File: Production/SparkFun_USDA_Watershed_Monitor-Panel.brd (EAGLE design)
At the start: 77.2 x 102.9 mm, 239 parts, among them J10 QWIIC_RIGHT_ANGLE, J3 QWIIC_RIGHT_ANGLE, J4 U.FL, J5 RJ45, J7 RJ45, J9 RJ45, Q1 20V/4.2A/52mΩ/1.4W, Q2 20V/0.2A/8MHz/1.2Ω/1Vth, Q3 20V/0.2A/8MHz/1.2Ω/1Vth, Q4 20V/0.2A/8MHz/1.2Ω/1Vth, Q5 20V/4.2A/52mΩ/1.4W, Q7 20V/4.2A/52mΩ/1.4W, U1 ESP-WROOM-3232D, U10 MMC5983MA_QFN16, U11 RFM9XRFM95, U12 NAU7802SOIC, U2 AP3429A, U3 MCP73831, U5 BME680, U6 9DoF IMU, U7 1.8V/100mA, U8 CH340C, U9 ISM330DHCX

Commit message: Add v10 production files
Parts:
- added BME_ADR1, BME_ADR2, BME_ADR3, BME_ADR4, BME_ADR5, CHG1, CHG2, CHG3, CHG4, CHG5, NAU_CAP1, NAU_CAP2, NAU_CAP3, NAU_CAP4, NAU_CAP5, PWR1, PWR2, PWR3, PWR4, PWR5, SHLD1, SHLD2, SHLD3, SHLD4, SHLD5: JUMPER-SMT_2_NC_TRACE_SILK, SparkFun-Jumpers:SMT-JUMPER_2_NC_TRACE_SILK
- added BOOT1, BOOT2, BOOT3, BOOT4, BOOT5, RESET1, RESET2, RESET3, RESET4, RESET5: MOMENTARY-SWITCH-SPST-SMD-4.6X2.8MM, SparkFun-Switches:TACTILE_SWITCH_SMD_4.6X2.8MM
- added C100, C101, C124, C125, C28, C29, C52, C53, C76, C77: 4.7uF, SparkFun-Capacitors:0603
- added C102, C103, C106, C107, C108, C109, C114, C115, C117, C126, C127, C130, C131, C132, C133, C138, C139, C141, C30, C31, C34, C35, C36, C37, C42, C43, C45, C54, C55, C58, C59, C60, C61, C66, C67, C69, C78, C79, C82, C83, C84, C85, C90, C91, C93: 0.1uF, SparkFun-Capacitors:0603
- added C104, C105, C128, C129, C32, C33, C56, C57, C80, C81: 1.0uF, SparkFun-Capacitors:0603
- added C110, C111, C112, C113, C134, C135, C136, C137, C38, C39, C40, C41, C62, C63, C64, C65, C86, C87, C88, C89: DNP, SparkFun-Capacitors:0603
- added C116, C140, C44, C68, C92: 330pF, SparkFun-Capacitors:0603
- added C118, C142, C46, C70, C94: 10uF, SparkFun-Capacitors:0603
- added C119, C121, C122, C143, C25, C26, C47, C49, C50, C71, C73, C74, C95, C97, C98: 22uF, SparkFun-Capacitors:0805
- added C120, C144, C48, C72, C96: 10nF, SparkFun-Capacitors:0603
- added C123, C27, C51, C75, C99: 22pF, SparkFun-Capacitors:0603
- added D10, D16, D22, D28, D34: BLUE, SparkFun-LED:LED-0603
- added D11, D12, D13, D17, D18, D19, D23, D24, D25, D29, D30, D31, D35, D36, D7: 3A/10V/280mV, SparkFun-DiscreteSemi:SOD-323
- added D14, D20, D26, D32, D8: DNP, SparkFun-LED:LED-0603
- added D15, D21, D27, D33, D9: Yellow, SparkFun-LED:LED-0603
- added FD10, FD11, FD12, FD13, FD14, FD15, FD16, FD17, FD18, FD19, FD20, FD21, FD22, FD23, FD24, FD5, FD6, FD7, FD8, FD9: FIDUCIAL1X2, SparkFun-Aesthetics:FIDUCIAL-1X2
- added H10, H11, H12, H13, H14, H15, H16, H17, H18, H19, H20, H21, H22, H23, H24, H5, H6, H7, H8, H9: STAND-OFF, SparkFun-Hardware:STAND-OFF
- added I2C1, I2C2, I2C3, I2C4, I2C5: JUMPER-SMT_3_2-NC_TRACE_SILK, SparkFun-Jumpers:SMT-JUMPER_3_2-NC_TRACE_SILK
- added ICM_ADR1, ICM_ADR2, ICM_ADR3, ICM_ADR4, ICM_ADR5, ISM_ADR1, ISM_ADR2, ISM_ADR3, ISM_ADR4, ISM_ADR5: JUMPER-SMT_2_NO_SILK, SparkFun-Jumpers:SMT-JUMPER_2_NO_SILK
- added ICM_INT1, ICM_INT2, ICM_INT3, ICM_INT4, ICM_INT5, ISM_INT10, ISM_INT11, ISM_INT12, ISM_INT3, ISM_INT4, ISM_INT5, ISM_INT6, ISM_INT7, ISM_INT8, ISM_INT9, MMC_INT1, MMC_INT2, MMC_INT3, MMC_INT4, MMC_INT5, NAU_INT1, NAU_INT2, NAU_INT3, NAU_INT4, NAU_INT5: JUMPER-SMT_3_1-NC_TRACE_SILK, SparkFun-Jumpers:SMT-JUMPER_3_1-NC_TRACE_SILK
- added J12, J24, J36, J48, J60, J72: 3-PIN SMD, SparkFun-Connectors:JST-3-SMD
- added J13, J25, J37, J49, J61: (no value), SparkFun-Connectors:USB-C-16P-2LAYER-PADS
- added J14, J26, J38, J50, J62: (no value), SparkFun-Connectors:JST-2-SMD
- added J15, J21, J27, J33, J39, J45, J51, J57, J63, J69: QWIIC_RIGHT_ANGLE, SparkFun-Connectors:JST04_1MM_RA
- added J16, J28, J40, J52, J64: U.FL, SparkFun-Connectors:U.FL
- added J17, J23, J29, J35, J41, J47, J53, J59, J65, J71: (no value), SparkFun-Connectors:1X02_NO_SILK
- added J18, J19, J20, J30, J31, J32, J42, J43, J44, J54, J55, J56, J66, J67, J68: RJ45, SparkFun-Connectors:RJ45-8
- added J22, J34, J46, J58, J70: (no value), SparkFun-Connectors:1X04_NO_SILK
- added L2, L3, L4, L5, L6: 2.2μH, SparkFun-Coils:INDUCTOR_4X4MM
- added LOGO10, LOGO11, LOGO15, LOGO16, LOGO20, LOGO21, LOGO25, LOGO26, LOGO30, LOGO6: SFE_LOGO_NAME_FLAME.1_INCH, SparkFun-Aesthetics:SFE_LOGO_NAME_FLAME_.1
- added LOGO12, LOGO17, LOGO22, LOGO27, LOGO7: OSHW-LOGOS, SparkFun-Aesthetics:OSHW-LOGO-S
- added LOGO13, LOGO14, LOGO18, LOGO19, LOGO23, LOGO24, LOGO28, LOGO29, LOGO8, LOGO9: QWIIC_LOGO_4MM, SparkFun-Aesthetics:QWIIC_4MM
- added MEAS1, MEAS2, MEAS3, MEAS4, MEAS5: JUMPER-COMBO_2_NC_TRACE, SparkFun-Jumpers:COMBO-JUMPER_2_NC_TRACE
- added Q10, Q12, Q17, Q18, Q21, Q23, Q28, Q29, Q32, Q34, Q39, Q40, Q43, Q45, Q50, Q51, Q54, Q56, Q61, Q62, Q65: 20V/4.2A/52mΩ/1.4W, SparkFun-DiscreteSemi:SOT23-3
- added Q11, Q13, Q14, Q15, Q19, Q20, Q22, Q24, Q25, Q26, Q30, Q31, Q33, Q35, Q36, Q37, Q41, Q42, Q44, Q46, Q47, Q48, Q52, Q53, Q55, Q57, Q58, Q59, Q63, Q64, Q66, Q8, Q9: 20V/0.2A/8MHz/1.2Ω/1Vth, SparkFun-DiscreteSemi:SOT-416FL
- added Q16, Q27, Q38, Q49, Q60: (no value), SparkFun-DiscreteSemi:SC70-6
- added R100, R131, R162, R38, R69: 4.7k, SparkFun-Resistors:0603
- added R101, R103, R104, R107, R108, R116, R121, R122, R132, R134, R135, R138, R139, R147, R152, R153, R163, R165, R166, R169, R170, R178, R183, R184, R29, R30, R39, R41, R42, R45, R46, R54, R59, R60, R70, R72, R73, R76, R77, R85, R90, R91: 2.2k, SparkFun-Resistors:0603
- added R102, R111, R133, R142, R164, R173, R40, R49, R71, R80: DNP, SparkFun-Resistors:0603
- added R105, R106, R109, R110, R117, R118, R119, R120, R123, R124, R127, R128, R130, R136, R137, R140, R141, R148, R149, R150, R151, R154, R155, R158, R159, R161, R167, R168, R171, R172, R179, R180, R181, R182, R185, R186, R28, R31, R34, R35, R37, R43, R44, R47, R48, R55, R56, R57, R58, R61, R62, R65, R66, R68, R74, R75, R78, R79, R86, R87, R88, R89, R92, R93, R96, R97, R99: 100k, SparkFun-Resistors:0603
- added R112, R113, R143, R144, R174, R175, R50, R51, R81, R82: 47, SparkFun-Resistors:0603
- added R114, R115, R145, R146, R176, R177, R52, R53, R83, R84: 10k, SparkFun-Resistors:0603
- added R125, R126, R156, R157, R32, R33, R63, R64, R94, R95: 5.1k, SparkFun-Resistors:0603
- added R129, R160, R36, R67, R98: 453k, SparkFun-Resistors:0603
- added TP2, TP3, TP4, TP5, TP6: TEST-POINT3X4, SparkFun-Connectors:PAD.03X.04
- added U$119, U$207, U$330, U$453, U$576, U$699: (no value), output:0X770
- added U$120, U$208, U$331, U$454, U$577, U$700: (no value), output:0X760
- added U$121, U$125, U$205, U$209, U$213, U$328, U$332, U$336, U$451, U$455, U$459, U$574, U$578, U$582, U$697, U$701, U$705, U$82: (no value), output:OPEN#0
- added U$122, U$126, U$206, U$210, U$214, U$329, U$333, U$337, U$452, U$456, U$460, U$575, U$579, U$583, U$698, U$702, U$706, U$83: (no value), output:CLOSED#0
- added U$123, U$215, U$338, U$461, U$584, U$707: (no value), output:0X6A0
- added U$124, U$216, U$339, U$462, U$585, U$708: (no value), output:0X6B0
- added U$127, U$211, U$334, U$457, U$580, U$703: (no value), output:0X690
- added U$128, U$212, U$335, U$458, U$581, U$704: (no value), output:0X680
- added U$129, U$260, U$383, U$506, U$629: (no value), output:RESET0
- added U$130, U$261, U$384, U$507, U$630: (no value), output:BOOT0
- added U$131, U$262, U$385, U$508, U$631: (no value), output:PWR0
- added U$132, U$263, U$386, U$509, U$632: (no value), output:STAT0
- added U$133, U$264, U$387, U$510, U$633: (no value), output:IO20
- added U$134, U$265, U$388, U$511, U$634: (no value), output:ORW0
- added U$135, U$266, U$389, U$512, U$635: (no value), output:OR0
- added U$136, U$267, U$390, U$513, U$636: (no value), output:GRW0
- added U$137, U$220, U$224, U$343, U$347, U$466, U$470, U$589, U$593, U$712, U$716: (no value), output:ICM0
- added U$138, U$217, U$225, U$232, U$235, U$340, U$348, U$355, U$358, U$463, U$471, U$478, U$481, U$586, U$594, U$601, U$604, U$709, U$717, U$724, U$727: (no value), output:X0
- added U$139, U$218, U$226, U$233, U$236, U$341, U$349, U$356, U$359, U$464, U$472, U$479, U$482, U$587, U$595, U$602, U$605, U$710, U$718, U$725, U$728: (no value), output:Y0
- added U$140, U$219, U$227, U$234, U$237, U$342, U$350, U$357, U$360, U$465, U$473, U$480, U$483, U$588, U$596, U$603, U$606, U$711, U$719, U$726, U$729: (no value), output:Z0
- added U$141, U$142, U$228, U$229, U$351, U$352, U$474, U$475, U$597, U$598, U$720, U$721: (no value), output:MAG0
- added U$143, U$144, U$230, U$231, U$353, U$354, U$476, U$477, U$599, U$600, U$722, U$723: (no value), output:A#G0
- added U$145, U$268, U$391, U$514, U$637: (no value), output:GR0
- added U$146, U$269, U$392, U$515, U$638: (no value), output:BLW0
- added U$147, U$270, U$393, U$516, U$639: (no value), output:BL0
- added U$148, U$271, U$394, U$517, U$640: (no value), output:BRW0
- added U$149, U$272, U$395, U$518, U$641: (no value), output:BR0
- added U$150, U$151, U$153, U$273, U$274, U$276, U$396, U$397, U$399, U$519, U$520, U$522, U$642, U$643, U$645: (no value), output:GND0
- added U$152, U$245, U$275, U$368, U$398, U$491, U$521, U$614, U$644, U$737: (no value), output:3V30
- added U$154, U$277, U$400, U$523, U$646: (no value), output:VDD0
- added U$155, U$278, U$401, U$524, U$647: (no value), output:A#0
- added U$156, U$279, U$402, U$525, U$648: (no value), output:A#1
- added U$157, U$280, U$403, U$526, U$649: (no value), output:B#0
- added U$158, U$281, U$404, U$527, U$650: (no value), output:B#1
- added U$159, U$282, U$405, U$528, U$651: (no value), output:E#0
- added U$160, U$283, U$406, U$529, U$652: (no value), output:E#1
- added U$161, U$284, U$407, U$530, U$653: (no value), output:#RJ45_COLORS#0
- added U$162, U$285, U$408, U$531, U$654: (no value), output:#PWR#0
- added U$163, U$286, U$409, U$532, U$655: (no value), output:IO250
- added U$164, U$287, U$410, U$533, U$656: (no value), output:IO330
- added U$165, U$288, U$411, U$534, U$657: (no value), output:IO170
- added U$166, U$289, U$412, U$535, U$658: (no value), output:IO180
- added U$167, U$290, U$413, U$536, U$659: (no value), output:IO190
- added U$168, U$291, U$414, U$537, U$660: (no value), output:I340
- added U$169, U$292, U$415, U$538, U$661: (no value), output:I350
- added U$170, U$293, U$416, U$539, U$662: (no value), output:I390
- added U$171, U$294, U$417, U$540, U$663: (no value), output:#IO19#0
- added U$172, U$295, U$418, U$541, U$664: (no value), output:#IO18#0
- added U$173, U$243, U$296, U$366, U$419, U$489, U$542, U$612, U$665, U$735: (no value), output:#IO17#0
- added U$174, U$297, U$420, U$543, U$666: (no value), output:#NAU_INT#0
- added U$175, U$298, U$421, U$544, U$667: (no value), output:#MMC_INT#0
- added U$176, U$299, U$422, U$545, U$668: (no value), output:#ISM_INT2#0
- added U$177, U$300, U$423, U$546, U$669: (no value), output:#ISM_INT1#0
- added U$178, U$301, U$424, U$547, U$670: (no value), output:#ICM_INT#0
- added U$179, U$302, U$425, U$548, U$671: (no value), output:#IO#0
- added U$180, U$303, U$426, U$549, U$672: (no value), output:##INT##0
- added U$181, U$304, U$427, U$550, U$673: (no value), output:#NOTES#0
- added U$182, U$305, U$428, U$551, U$674: (no value), output:IO230
- added U$183, U$185, U$306, U$308, U$429, U$431, U$552, U$554, U$675, U$677: (no value), output:#GND_#0
- added U$184, U$186, U$307, U$309, U$430, U$432, U$553, U$555, U$676, U$678: (no value), output:#_GND#0
- added U$187, U$310, U$433, U$556, U$679: (no value), output:#3V3_#0
- added U$188, U$311, U$434, U$557, U$680: (no value), output:#SDA_#0
- added U$189, U$312, U$435, U$558, U$681: (no value), output:#SCL_#0
- added U$190, U$313, U$436, U$559, U$682: (no value), output:#_SCL#1
- added U$191, U$314, U$437, U$560, U$683: (no value), output:#_SDA#2
- added U$192, U$315, U$438, U$561, U$684: (no value), output:#_3V3#0
- added U$193, U$196, U$316, U$319, U$439, U$442, U$562, U$565, U$685, U$688: (no value), output:#LOAD_CELL#0
- added U$194, U$197, U$317, U$320, U$440, U$443, U$563, U$566, U$686, U$689: (no value), output:#GPIO_A#0
- added U$195, U$198, U$318, U$321, U$441, U$444, U$564, U$567, U$687, U$690: (no value), output:#GPIO_B#0
- added U$199, U$247, U$322, U$370, U$445, U$493, U$568, U$616, U$691: (no value), output:USDA0
- added U$200, U$248, U$323, U$371, U$446, U$494, U$569, U$617, U$692: (no value), output:WATERSHED0
- added U$201, U$249, U$324, U$372, U$447, U$495, U$570, U$618, U$693: (no value), output:MONITOR0
- added U$202, U$325, U$448, U$571, U$694: (no value), output:NC0
- added U$203, U$326, U$449, U$572, U$695: (no value), output:#5V_IN_#0
- added U$204, U$327, U$450, U$573, U$696: (no value), output:#_5V_IN#0
- added U$221, U$344, U$467, U$590, U$713: (no value), output:ISM0
- added U$222, U$345, U$468, U$591, U$714: (no value), output:MMC0
- added U$223, U$346, U$469, U$592, U$715: (no value), output:IMU_AXES0
- added U$238, U$361, U$484, U$607, U$730: (no value), output:I360
- added U$239, U$362, U$485, U$608, U$731: (no value), output:VOUT0
- added U$240, U$363, U$486, U$609, U$732: (no value), output:#GPS#0
- added U$241, U$364, U$487, U$610, U$733: (no value), output:GND3
- added U$242, U$246, U$365, U$369, U$488, U$492, U$611, U$615, U$734, U$738: (no value), output:VO0
- added U$244, U$367, U$490, U$613, U$736: (no value), output:#IO23#0
- added U$250, U$373, U$496, U$619: (no value), output:#MEAS#0
- added U$251, U$374, U$497, U$620: (no value), output:#CHG#0
- added U$252, U$375, U$498, U$621: (no value), output:#I2C#0
- added U$253, U$376, U$499, U$622: (no value), output:CHG0
- added U$254, U$377, U$500, U$623: (no value), output:#CAP#0
- added U$255, U$378, U$501, U$624: (no value), output:#BME_ADR#0
- added U$256, U$379, U$502, U$625: (no value), output:#ICM_ADR#0
- added U$257, U$380, U$503, U$626: (no value), output:#ISM_ADR#0
- added U$258, U$381, U$504, U$627: (no value), output:#BATTERY#0
- added U$259, U$382, U$505, U$628: (no value), output:#SHLD#0
- added U13, U24, U35, U46, U57: AP3429A, SparkFun-IC-Power:SOT23-5
- added U14, U25, U36, U47, U58: MCP73831, SparkFun-IC-Power:SOT23-5
- added U15, U26, U37, U48, U59: BME680, SparkFun-Sensors:LGA3.0X3.0
- added U16, U27, U38, U49, U60: 9DoF IMU, SparkFun-Sensors:QFN24-3X3-ICM-20948
- added U17, U28, U39, U50, U61: 1.8V/100mA, SparkFun-IC-Power:SC70
- added U18, U29, U40, U51, U62: CH340C, SparkFun-IC-Comms:SO016
- added U19, U30, U41, U52, U63: DNP, SparkFun-Sensors:LGA-14L
- added U20, U31, U42, U53, U64: DNP, SparkFun-Sensors:LGA-16-3X3MM-4X4PINS
- added U21, U32, U43, U54, U65: RFM9XRFM95, SparkFun-RF:RFM95
- added U22, U33, U44, U55, U66: NAU7802SOIC, SparkFun-IC-Conversion:SO16
- added U23, U34, U4, U45, U56: ESP-WROOM-3232D, SparkFun-RF:ESP-WROOM-32D
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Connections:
- net !RFM_CS! renamed ESP_IO15/!RFM_CS!
- net !RFM_RST! renamed ESP_IO5/!RFM_RST!
- net ESP_IO0_BOOT renamed ESP_IO0/BOOT
- net ESP_RX renamed ESP_IO3/ESP_RX
- net ESP_TX renamed ESP_IO1/ESP_TX
- net PICO renamed ESP_IO13/PICO
- net POCI renamed ESP_IO12/POCI
- net RFM_IO0 renamed ESP_IO27/RFM_IO0
- net RFM_IO1 renamed ESP_IO26/RFM_IO1
- net SCK renamed ESP_IO14/SCK
- net STAT renamed ESP_IO2/STAT
- net V_BATT_2 renamed ESP_IO32/V_BATT_2
- removed net ESP_I36: J7.5, U1.4
- removed net ESP_INT_COM: ICM_INT.3, ISM_INT1.3, ISM_INT2.3, MMC_INT.3, NAU_INT.3, U1.26
- removed net SCL: J10.4, J3.4, J8.1, Q3.3, R11.1, U1.36, U10.1, U12.13, U5.4, U9.P13
- removed net SDA: J10.3, J3.3, J8.2, Q2.3, R12.1, U1.33, U10.16, U12.14, U5.3, U9.P14
- new net 1.8V1: C33.1, C34.1, C35.1, Q13.1, Q14.1, R44.2, R45.2, R46.2, TP2.1, U16.13, U16.22, U16.8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
- new net 1.8V2: C57.1, C58.1, C59.1, Q24.1, Q25.1, R75.2, R76.2, R77.2, TP3.1, U27.13, U27.22, U27.8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
- new net 1.8V3: C81.1, C82.1, C83.1, Q35.1, Q36.1, R106.2, R107.2, R108.2, TP4.1, U38.13, U38.22, U38.8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
- new net 1.8V4: C105.1, C106.1, C107.1, Q46.1, Q47.1, R137.2, R138.2, R139.2, TP5.1, U49.13, U49.22, U49.8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
- new net 1.8V5: C129.1, C130.1, C131.1, Q57.1, Q58.1, R168.2, R169.2, R170.2, TP6.1, U60.13, U60.22, U60.8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
- new net 3.3V1: C26.1, C27.2, C47.1, D8.A, I2C1.2, J15.2, J19.7, J20.7, J22.3, L2.P$2, Q18.2, Q21.2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
- new net 3.3V2: C50.1, C51.2, C71.1, D14.A, I2C2.2, J27.2, J31.7, J32.7, J34.3, L3.P$2, Q29.2, Q32.2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
- new net 3.3V3: C74.1, C75.2, C95.1, D20.A, I2C3.2, J39.2, J43.7, J44.7, J46.3, L4.P$2, Q40.2, Q43.2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
- new net 3.3V4: C119.1, C98.1, C99.2, D26.A, I2C4.2, J51.2, J55.7, J56.7, J58.3, L5.P$2, Q51.2, Q54.2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
- new net 3.3V5: C122.1, C123.2, C143.1, D32.A, I2C5.2, J63.2, J67.7, J68.7, J70.3, L6.P$2, Q62.2, Q65.2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
- new net 3V3_EN1: R35.2, U13.1
- new net 3V3_EN2: R66.2, U24.1
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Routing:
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- added copper zone on layer 1, net 3.3V1
- added copper zone on layer 16, net 3.3V1
- added copper zone on layer 1, net 3.3V2
- added copper zone on layer 16, net 3.3V2
- added copper zone on layer 1, net 3.3V3
- added copper zone on layer 16, net 3.3V3
- added copper zone on layer 1, net 3.3V4
- added copper zone on layer 16, net 3.3V4
- added copper zone on layer 1, net 3.3V5
- added copper zone on layer 16, net 3.3V5
- added copper zone on layer 1, net GND1
- added copper zone on layer 16, net GND1
- added copper zone on layer 1, net GND10
- added copper zone on layer 16, net GND10
- added copper zone on layer 16, net GND11
- added copper zone on layer 16, net GND3
- added copper zone on layer 1, net GND4
- added copper zone on layer 16, net GND4
- added copper zone on layer 16, net GND5
- added copper zone on layer 1, net GND6
- added copper zone on layer 16, net GND6
- added copper zone on layer 16, net GND7
- added copper zone on layer 1, net GND8
- added copper zone on layer 16, net GND8
- added copper zone on layer 16, net GND9
- added copper zone on layer 1, net SHLD1
- added copper zone on layer 16, net SHLD1
- added copper zone on layer 1, net SHLD2
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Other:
- board size 77.2 x 102.9 mm -> 141.2 x 245.1 mm
- board text added: "v10"
- board text removed: "v01"

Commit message: Change DIO-14072 for DIO-11623
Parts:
- D1, D11, D12, D13, D17, D18, D19, D23, D24, D25, D29, D30, D31, D35, D36, D5, D6, D7: value 3A/10V/280mV -> 1A/23V/620mV

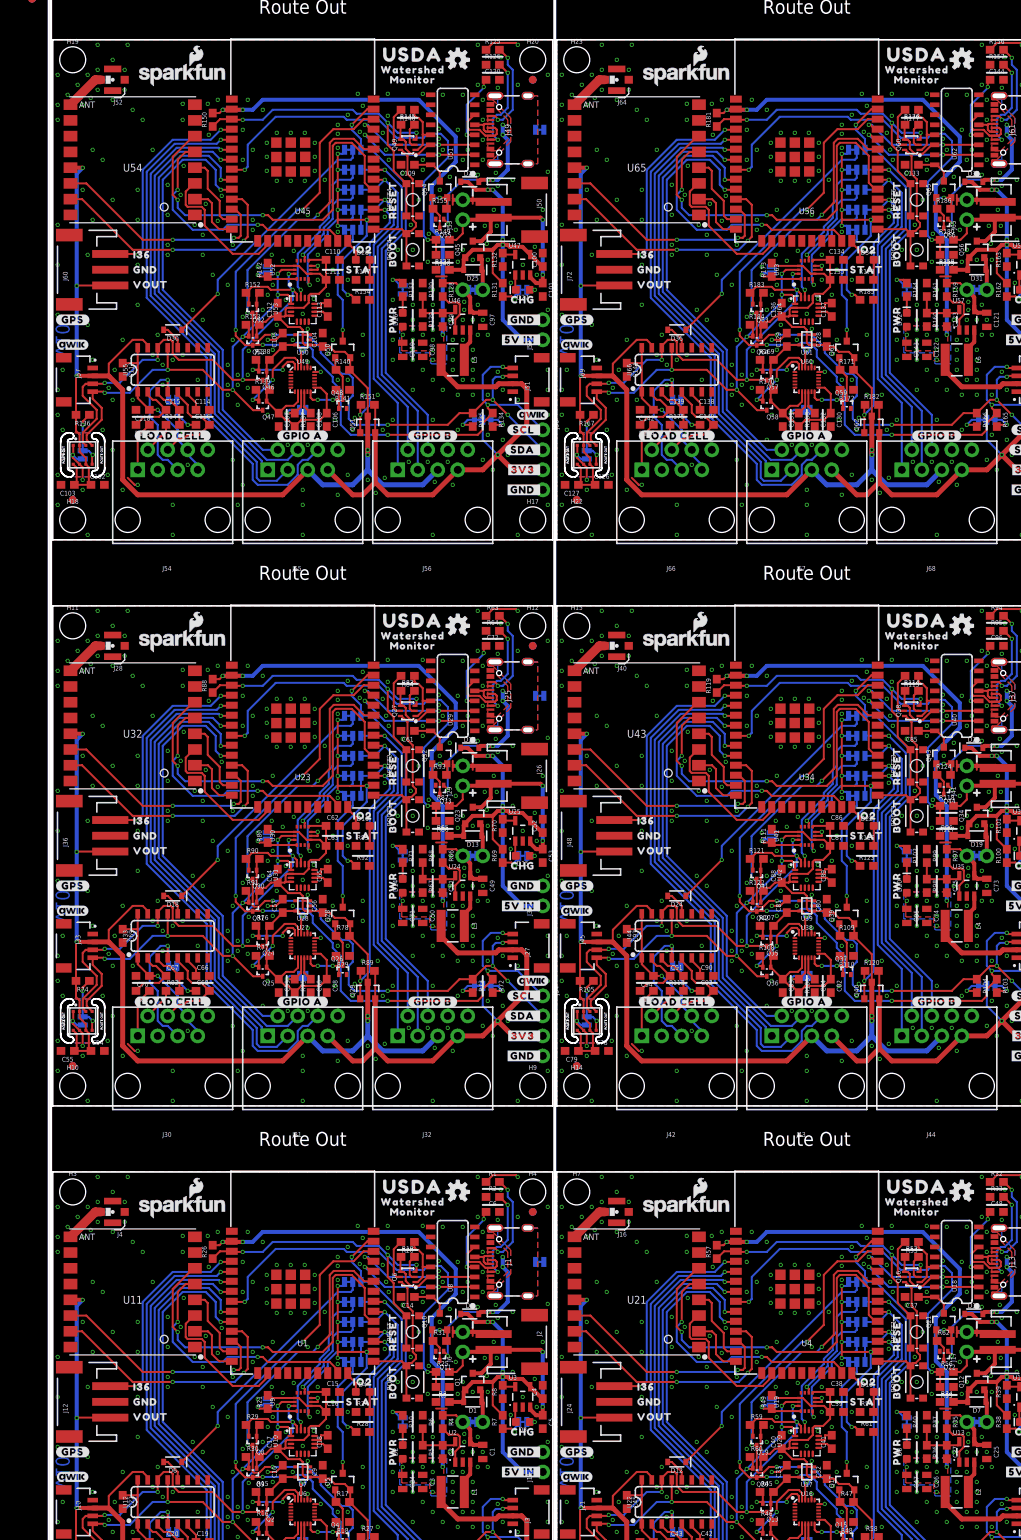
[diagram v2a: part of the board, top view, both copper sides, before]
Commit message: v11 updates
Bump version number to v11
Remove USDA from silkscreen
Repanelize
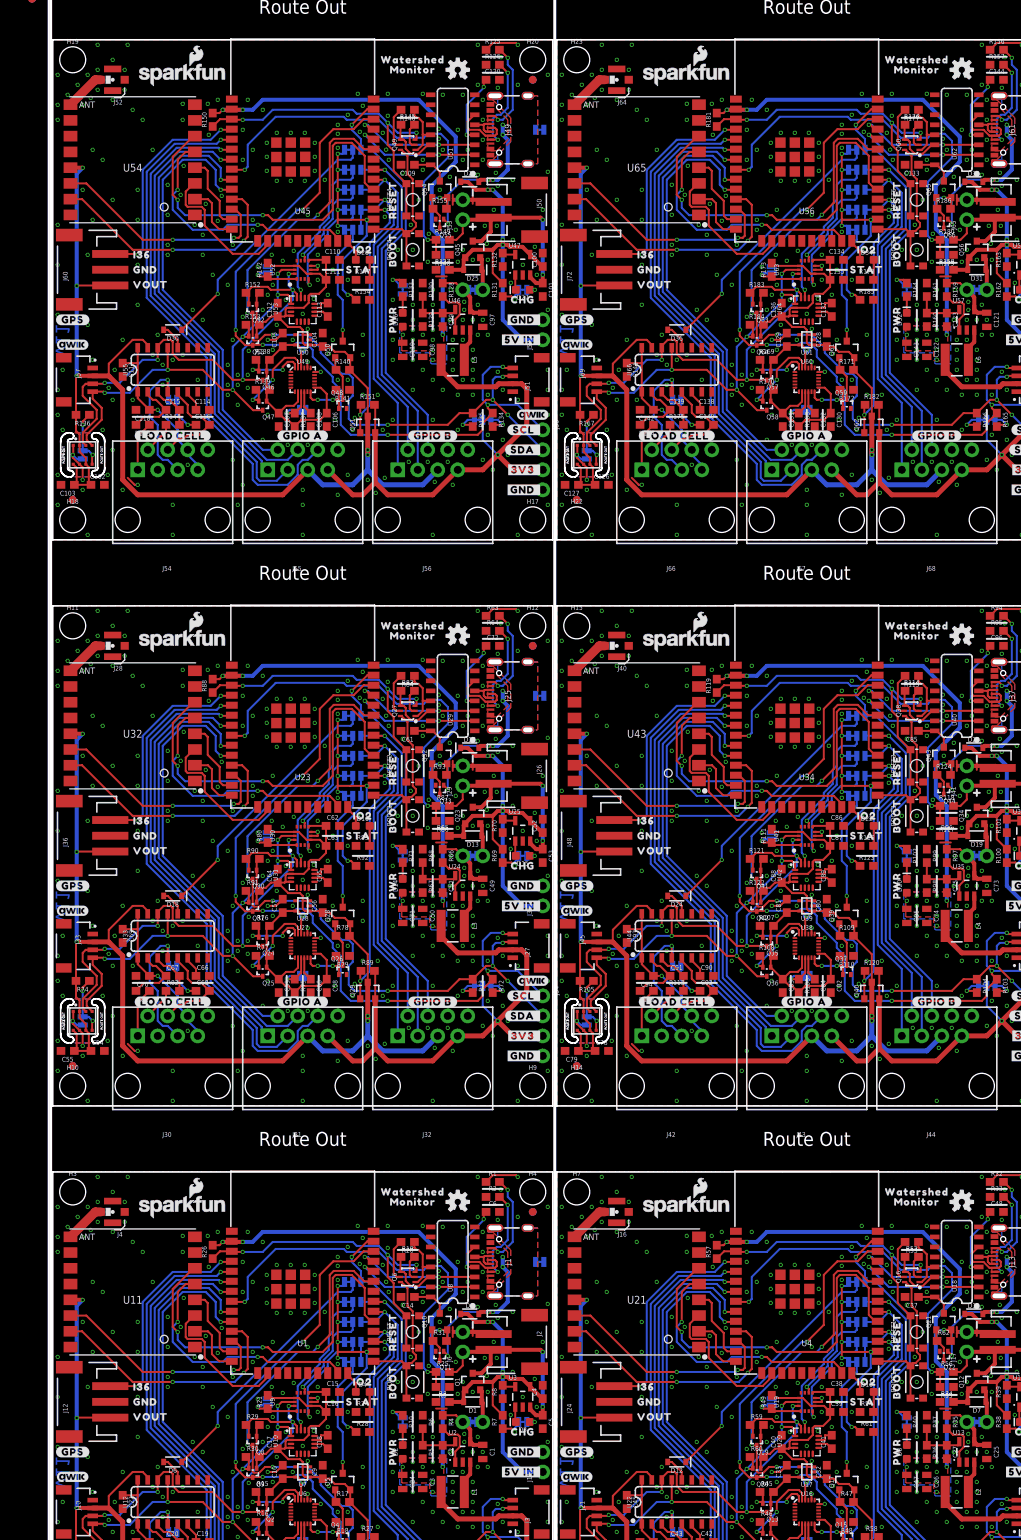
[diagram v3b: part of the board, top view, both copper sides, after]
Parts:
- removed U$727: (no value), output:X0
- removed U$728: (no value), output:Y0
- removed U$729: (no value), output:Z0
- removed U$730: (no value), output:I360
- removed U$731: (no value), output:VOUT0
- removed U$732: (no value), output:#GPS#0
- removed U$733: (no value), output:GND3
- removed U$734, U$738: (no value), output:VO0
- removed U$735: (no value), output:#IO17#0
- removed U$736: (no value), output:#IO23#0
- removed U$737: (no value), output:3V30
- U$1: device output:USDA0 -> output:WATERSHED0
- U$101: device output:#ICM_ADR#0 -> output:#BATTERY#0
- U$107: device output:#ISM_ADR#0 -> output:#SHLD#0
- U$108: device output:#BATTERY#0 -> output:RESET0
- U$109: device output:#SHLD#0 -> output:BOOT0
- U$114: device output:USDA0 -> output:PWR0
- U$129: device output:RESET0 -> output:STAT0
- U$130: device output:BOOT0 -> output:IO20
- U$131: device output:PWR0 -> output:ORW0
- U$132: device output:STAT0 -> output:OR0
- U$133: device output:IO20 -> output:GRW0
- U$134: device output:ORW0 -> output:GR0
- U$135: device output:OR0 -> output:BLW0
- U$136: device output:GRW0 -> output:BL0
- U$145: device output:GR0 -> output:BRW0
- U$146: device output:BLW0 -> output:BR0
- U$147: device output:BL0 -> output:GND0
- U$148, U$271: device output:BRW0 -> output:GND0
- U$149: device output:BR0 -> output:3V30
- U$151: device output:GND0 -> output:VDD0
- U$152: device output:3V30 -> output:A#0
- U$153, U$274: device output:GND0 -> output:A#1
- U$154: device output:VDD0 -> output:B#0
- U$155: device output:A#0 -> output:B#1
- U$156: device output:A#1 -> output:E#0
- U$157: device output:B#0 -> output:E#1
- U$158: device output:B#1 -> output:#RJ45_COLORS#0
- U$159: device output:E#0 -> output:#PWR#0
- U$160: device output:E#1 -> output:IO250
- U$161: device output:#RJ45_COLORS#0 -> output:IO330
- U$162: device output:#PWR#0 -> output:IO170
- U$163: device output:IO250 -> output:IO180
- U$164: device output:IO330 -> output:IO190
- U$165: device output:IO170 -> output:I340
- U$166: device output:IO180 -> output:I350
- U$167: device output:IO190 -> output:I390
- U$168: device output:I340 -> output:#IO19#0
- U$169: device output:I350 -> output:#IO18#0
- U$170: device output:I390 -> output:#IO17#0
- U$171: device output:#IO19#0 -> output:#NAU_INT#0
- U$172: device output:#IO18#0 -> output:#MMC_INT#0
- U$173: device output:#IO17#0 -> output:#ISM_INT2#0
- U$174: device output:#NAU_INT#0 -> output:#ISM_INT1#0
- U$175: device output:#MMC_INT#0 -> output:#ICM_INT#0
- U$176: device output:#ISM_INT2#0 -> output:#IO#0
- U$177: device output:#ISM_INT1#0 -> output:##INT##0
- U$178: device output:#ICM_INT#0 -> output:#NOTES#0
- U$179: device output:#IO#0 -> output:IO230
- U$180, U$303: device output:##INT##0 -> output:#GND_#0
- U$181, U$304: device output:#NOTES#0 -> output:#_GND#0
- U$182: device output:IO230 -> output:#GND_#0
- U$183: device output:#GND_#0 -> output:#_GND#0
- U$184: device output:#_GND#0 -> output:#3V3_#0
- U$185, U$306: device output:#GND_#0 -> output:#SDA_#0
- U$186, U$307: device output:#_GND#0 -> output:#SCL_#0
- U$187: device output:#3V3_#0 -> output:#_SCL#1
- U$188: device output:#SDA_#0 -> output:#_SDA#2
- U$189: device output:#SCL_#0 -> output:#_3V3#0
- U$190: device output:#_SCL#1 -> output:#LOAD_CELL#0
- U$191: device output:#_SDA#2 -> output:#GPIO_A#0
- U$192: device output:#_3V3#0 -> output:#GPIO_B#0
- U$196: device output:#LOAD_CELL#0 -> output:WATERSHED0
- U$197: device output:#GPIO_A#0 -> output:MONITOR0
- U$198: device output:#GPIO_B#0 -> output:NC0
- U$199: device output:USDA0 -> output:#5V_IN_#0
- U$200: device output:WATERSHED0 -> output:#_5V_IN#0
- U$201, U$447, U$693: device output:MONITOR0 -> output:OPEN#0
- U$202, U$448, U$694: device output:NC0 -> output:CLOSED#0
- U$203: device output:#5V_IN_#0 -> output:0X770
- U$204: device output:#_5V_IN#0 -> output:0X760
- U$207: device output:0X770 -> output:0X690
- U$208: device output:0X760 -> output:0X680
- U$211: device output:0X690 -> output:0X6A0
- U$212: device output:0X680 -> output:0X6B0
- U$213, U$455, U$697, U$705: device output:OPEN#0 -> output:X0
- U$214, U$456, U$698, U$706: device output:CLOSED#0 -> output:Y0
- U$215, U$707: device output:0X6A0 -> output:Z0
- U$216, U$462: device output:0X6B0 -> output:ICM0
- U$217: device output:X0 -> output:ISM0
- U$218: device output:Y0 -> output:MMC0
- U$219: device output:Z0 -> output:IMU_AXES0
- U$221: device output:ISM0 -> output:X0
- U$222: device output:MMC0 -> output:Y0
- U$223: device output:IMU_AXES0 -> output:Z0
- U$224, U$466: device output:ICM0 -> output:MAG0
- U$225, U$709: device output:X0 -> output:MAG0
- U$226, U$710: device output:Y0 -> output:A#G0
- U$227, U$711: device output:Z0 -> output:A#G0
- U$228, U$352: device output:MAG0 -> output:X0
- U$229, U$474: device output:MAG0 -> output:Y0
- U$230, U$354: device output:A#G0 -> output:Z0
- U$231: device output:A#G0 -> output:X0
- U$232, U$471: device output:X0 -> output:Y0
- U$233, U$472: device output:Y0 -> output:Z0
- U$234: device output:Z0 -> output:I360
- U$235: device output:X0 -> output:VOUT0
- U$236: device output:Y0 -> output:#GPS#0
- U$237: device output:Z0 -> output:GND3
- U$238, U$484: device output:I360 -> output:VO0
- U$239: device output:VOUT0 -> output:#IO17#0
- U$240: device output:#GPS#0 -> output:#IO23#0
- U$241: device output:GND3 -> output:3V30
- U$243: device output:#IO17#0 -> output:WATERSHED0
- U$244: device output:#IO23#0 -> output:MONITOR0
- U$245: device output:3V30 -> output:#MEAS#0
- U$246, U$488: device output:VO0 -> output:#CHG#0
- U$247: device output:USDA0 -> output:#I2C#0
- U$248: device output:WATERSHED0 -> output:CHG0
- U$249: device output:MONITOR0 -> output:#CAP#0
- U$250: device output:#MEAS#0 -> output:#BME_ADR#0
- U$251: device output:#CHG#0 -> output:#ICM_ADR#0
- U$252: device output:#I2C#0 -> output:#ISM_ADR#0
- U$253: device output:CHG0 -> output:#BATTERY#0
- U$254: device output:#CAP#0 -> output:#SHLD#0
- U$255: device output:#BME_ADR#0 -> output:RESET0
- U$256: device output:#ICM_ADR#0 -> output:BOOT0
- U$257: device output:#ISM_ADR#0 -> output:PWR0
- U$258: device output:#BATTERY#0 -> output:STAT0
- U$259: device output:#SHLD#0 -> output:IO20
- U$260: device output:RESET0 -> output:ORW0
- U$261: device output:BOOT0 -> output:OR0
- U$262: device output:PWR0 -> output:GRW0
- U$263: device output:STAT0 -> output:GR0
- U$264: device output:IO20 -> output:BLW0
- U$265: device output:ORW0 -> output:BL0
- U$266: device output:OR0 -> output:BRW0
- U$267: device output:GRW0 -> output:BR0
- U$268: device output:GR0 -> output:GND0
- U$269, U$392: device output:BLW0 -> output:GND0
- U$270: device output:BL0 -> output:3V30
- U$272: device output:BR0 -> output:VDD0
- U$273: device output:GND0 -> output:A#0
- U$275: device output:3V30 -> output:B#0
- U$276, U$397: device output:GND0 -> output:B#1
- U$277: device output:VDD0 -> output:E#0
- U$278: device output:A#0 -> output:E#1
- U$279: device output:A#1 -> output:#RJ45_COLORS#0
- U$280: device output:B#0 -> output:#PWR#0
- U$281: device output:B#1 -> output:IO250
- U$282: device output:E#0 -> output:IO330
- U$283: device output:E#1 -> output:IO170
- U$284: device output:#RJ45_COLORS#0 -> output:IO180
- U$285: device output:#PWR#0 -> output:IO190
- U$286: device output:IO250 -> output:I340
- U$287: device output:IO330 -> output:I350
- U$288: device output:IO170 -> output:I390
- U$289: device output:IO180 -> output:#IO19#0
- U$290: device output:IO190 -> output:#IO18#0
- U$291: device output:I340 -> output:#IO17#0
- U$292: device output:I350 -> output:#NAU_INT#0
- U$293: device output:I390 -> output:#MMC_INT#0
- U$294: device output:#IO19#0 -> output:#ISM_INT2#0
- U$295: device output:#IO18#0 -> output:#ISM_INT1#0
- U$296: device output:#IO17#0 -> output:#ICM_INT#0
- U$297: device output:#NAU_INT#0 -> output:#IO#0
- U$298: device output:#MMC_INT#0 -> output:##INT##0
- U$299: device output:#ISM_INT2#0 -> output:#NOTES#0
- U$300: device output:#ISM_INT1#0 -> output:IO230
- U$301, U$424: device output:#ICM_INT#0 -> output:#GND_#0
- U$302, U$425: device output:#IO#0 -> output:#_GND#0
- U$305: device output:IO230 -> output:#3V3_#0
- U$308, U$429: device output:#GND_#0 -> output:#_SCL#1
- U$309, U$430: device output:#_GND#0 -> output:#_SDA#2
- U$310: device output:#3V3_#0 -> output:#_3V3#0
- U$311: device output:#SDA_#0 -> output:#LOAD_CELL#0
- U$312: device output:#SCL_#0 -> output:#GPIO_A#0
- U$313: device output:#_SCL#1 -> output:#GPIO_B#0
- U$314: device output:#_SDA#2 -> output:#LOAD_CELL#0
- U$315: device output:#_3V3#0 -> output:#GPIO_A#0
- U$316: device output:#LOAD_CELL#0 -> output:#GPIO_B#0
- U$317: device output:#GPIO_A#0 -> output:WATERSHED0
- U$318: device output:#GPIO_B#0 -> output:MONITOR0
- U$319: device output:#LOAD_CELL#0 -> output:NC0
- U$320: device output:#GPIO_A#0 -> output:#5V_IN_#0
- U$321: device output:#GPIO_B#0 -> output:#_5V_IN#0
- U$322, U$568: device output:USDA0 -> output:OPEN#0
- U$323, U$569: device output:WATERSHED0 -> output:CLOSED#0
- U$324: device output:MONITOR0 -> output:0X770
- U$325: device output:NC0 -> output:0X760
- U$326, U$572: device output:#5V_IN_#0 -> output:OPEN#0
- U$327, U$573: device output:#_5V_IN#0 -> output:CLOSED#0
- U$328: device output:OPEN#0 -> output:0X690
- U$329: device output:CLOSED#0 -> output:0X680
- U$330: device output:0X770 -> output:OPEN#0
- U$331: device output:0X760 -> output:CLOSED#0
- U$332, U$574: device output:OPEN#0 -> output:0X6A0
- U$333, U$575: device output:CLOSED#0 -> output:0X6B0
- U$334: device output:0X690 -> output:X0
- U$335: device output:0X680 -> output:Y0
- U$336, U$578: device output:OPEN#0 -> output:Z0
- U$337, U$579, U$583: device output:CLOSED#0 -> output:ICM0
- U$338: device output:0X6A0 -> output:ISM0
- U$339: device output:0X6B0 -> output:MMC0
- U$340: device output:X0 -> output:IMU_AXES0
- U$341: device output:Y0 -> output:ICM0
- U$342, U$473: device output:Z0 -> output:X0
- U$343, U$716: device output:ICM0 -> output:Y0
- U$344: device output:ISM0 -> output:Z0
- U$345: device output:MMC0 -> output:MAG0
- U$346: device output:IMU_AXES0 -> output:MAG0
- U$347, U$589: device output:ICM0 -> output:A#G0
- U$348: device output:X0 -> output:A#G0
- U$349: device output:Y0 -> output:X0
- U$350: device output:Z0 -> output:Y0
- U$351, U$475: device output:MAG0 -> output:Z0
- U$353: device output:A#G0 -> output:Y0
- U$355: device output:X0 -> output:I360
- U$356: device output:Y0 -> output:VOUT0
- U$357: device output:Z0 -> output:#GPS#0
- U$358: device output:X0 -> output:GND3
- U$359, U$605: device output:Y0 -> output:VO0
- U$360: device output:Z0 -> output:#IO17#0
- U$361: device output:I360 -> output:#IO23#0
- U$362: device output:VOUT0 -> output:3V30
- U$363: device output:#GPS#0 -> output:VO0
- U$364: device output:GND3 -> output:WATERSHED0
- U$365: device output:VO0 -> output:MONITOR0
- U$366: device output:#IO17#0 -> output:#MEAS#0
- U$367: device output:#IO23#0 -> output:#CHG#0
- U$368: device output:3V30 -> output:#I2C#0
- U$369, U$611: device output:VO0 -> output:CHG0
- U$370: device output:USDA0 -> output:#CAP#0
- U$371: device output:WATERSHED0 -> output:#BME_ADR#0
- U$372: device output:MONITOR0 -> output:#ICM_ADR#0
- U$373: device output:#MEAS#0 -> output:#ISM_ADR#0
- U$374: device output:#CHG#0 -> output:#BATTERY#0
- U$375: device output:#I2C#0 -> output:#SHLD#0
- U$376: device output:CHG0 -> output:RESET0
- U$377: device output:#CAP#0 -> output:BOOT0
- U$378: device output:#BME_ADR#0 -> output:PWR0
- U$379: device output:#ICM_ADR#0 -> output:STAT0
- U$380: device output:#ISM_ADR#0 -> output:IO20
- U$381: device output:#BATTERY#0 -> output:ORW0
- U$382: device output:#SHLD#0 -> output:OR0
- U$383: device output:RESET0 -> output:GRW0
- U$384: device output:BOOT0 -> output:GR0
- U$385: device output:PWR0 -> output:BLW0
- U$386: device output:STAT0 -> output:BL0
- U$387: device output:IO20 -> output:BRW0
- U$388: device output:ORW0 -> output:BR0
- U$389: device output:OR0 -> output:GND0
- U$390, U$513: device output:GRW0 -> output:GND0
- U$391: device output:GR0 -> output:3V30
- U$393: device output:BL0 -> output:VDD0
- U$394: device output:BRW0 -> output:A#0
- U$395: device output:BR0 -> output:A#1
- U$396: device output:GND0 -> output:B#0
- U$398: device output:3V30 -> output:E#0
- U$399, U$520: device output:GND0 -> output:E#1
- U$400: device output:VDD0 -> output:#RJ45_COLORS#0
- U$401: device output:A#0 -> output:#PWR#0
- U$402: device output:A#1 -> output:IO250
- U$403: device output:B#0 -> output:IO330
- U$404: device output:B#1 -> output:IO170
- U$405: device output:E#0 -> output:IO180
- U$406: device output:E#1 -> output:IO190
- U$407: device output:#RJ45_COLORS#0 -> output:I340
- U$408: device output:#PWR#0 -> output:I350
- U$409: device output:IO250 -> output:I390
- U$410: device output:IO330 -> output:#IO19#0
- U$411: device output:IO170 -> output:#IO18#0
- U$412: device output:IO180 -> output:#IO17#0
- U$413: device output:IO190 -> output:#NAU_INT#0
- U$414: device output:I340 -> output:#MMC_INT#0
- U$415: device output:I350 -> output:#ISM_INT2#0
- U$416: device output:I390 -> output:#ISM_INT1#0
- U$417: device output:#IO19#0 -> output:#ICM_INT#0
- U$418: device output:#IO18#0 -> output:#IO#0
- U$419: device output:#IO17#0 -> output:##INT##0
- U$420: device output:#NAU_INT#0 -> output:#NOTES#0
- U$421: device output:#MMC_INT#0 -> output:IO230
- U$422, U$545: device output:#ISM_INT2#0 -> output:#GND_#0
- U$423, U$546: device output:#ISM_INT1#0 -> output:#_GND#0
- U$426: device output:##INT##0 -> output:#3V3_#0
- U$427: device output:#NOTES#0 -> output:#SDA_#0
- U$428: device output:IO230 -> output:#SCL_#0
- U$431, U$552: device output:#GND_#0 -> output:#_3V3#0
- U$432, U$553: device output:#_GND#0 -> output:#LOAD_CELL#0
- U$433: device output:#3V3_#0 -> output:#GPIO_A#0
- U$434: device output:#SDA_#0 -> output:#GPIO_B#0
- U$435: device output:#SCL_#0 -> output:#LOAD_CELL#0
- U$436: device output:#_SCL#1 -> output:#GPIO_A#0
- U$437: device output:#_SDA#2 -> output:#GPIO_B#0
- U$438: device output:#_3V3#0 -> output:WATERSHED0
- U$439: device output:#LOAD_CELL#0 -> output:MONITOR0
- U$440: device output:#GPIO_A#0 -> output:NC0
- U$441: device output:#GPIO_B#0 -> output:#5V_IN_#0
- U$442: device output:#LOAD_CELL#0 -> output:#_5V_IN#0
- U$443, U$689: device output:#GPIO_A#0 -> output:OPEN#0
- U$444, U$690: device output:#GPIO_B#0 -> output:CLOSED#0
- U$445: device output:USDA0 -> output:0X770
- U$446: device output:WATERSHED0 -> output:0X760
- U$449: device output:#5V_IN_#0 -> output:0X690
- U$450: device output:#_5V_IN#0 -> output:0X680
- U$453: device output:0X770 -> output:0X6A0
- U$454: device output:0X760 -> output:0X6B0
- U$457: device output:0X690 -> output:Z0
- U$458, U$704: device output:0X680 -> output:ICM0
- U$459, U$701: device output:OPEN#0 -> output:ISM0
- U$460, U$702: device output:CLOSED#0 -> output:MMC0
- U$461: device output:0X6A0 -> output:IMU_AXES0
- U$467: device output:ISM0 -> output:MAG0
- U$468: device output:MMC0 -> output:A#G0
- U$469: device output:IMU_AXES0 -> output:A#G0
- U$470, U$712: device output:ICM0 -> output:X0
- U$476: device output:A#G0 -> output:I360
- U$477: device output:A#G0 -> output:VOUT0
- U$478: device output:X0 -> output:#GPS#0
- U$479: device output:Y0 -> output:GND3
- U$480, U$726: device output:Z0 -> output:VO0
- U$481: device output:X0 -> output:#IO17#0
- U$482: device output:Y0 -> output:#IO23#0
- U$483: device output:Z0 -> output:3V30
- U$485: device output:VOUT0 -> output:WATERSHED0
- U$486: device output:#GPS#0 -> output:MONITOR0
- U$487: device output:GND3 -> output:#MEAS#0
- U$489: device output:#IO17#0 -> output:#I2C#0
- U$49: device output:USDA0 -> output:MONITOR0
- U$490: device output:#IO23#0 -> output:CHG0
- U$491: device output:3V30 -> output:#CAP#0
- U$492: device output:VO0 -> output:#BME_ADR#0
- U$493: device output:USDA0 -> output:#ICM_ADR#0
- U$494: device output:WATERSHED0 -> output:#ISM_ADR#0
- U$495: device output:MONITOR0 -> output:#BATTERY#0
- U$496: device output:#MEAS#0 -> output:#SHLD#0
- U$497: device output:#CHG#0 -> output:RESET0
- U$498: device output:#I2C#0 -> output:BOOT0
- U$499: device output:CHG0 -> output:PWR0
- U$500: device output:#CAP#0 -> output:STAT0
- U$501: device output:#BME_ADR#0 -> output:IO20
- U$502: device output:#ICM_ADR#0 -> output:ORW0
- U$503: device output:#ISM_ADR#0 -> output:OR0
- U$504: device output:#BATTERY#0 -> output:GRW0
- U$505: device output:#SHLD#0 -> output:GR0
- U$506: device output:RESET0 -> output:BLW0
- U$507: device output:BOOT0 -> output:BL0
- U$508: device output:PWR0 -> output:BRW0
- U$509: device output:STAT0 -> output:BR0
- U$510: device output:IO20 -> output:GND0
- U$511, U$634: device output:ORW0 -> output:GND0
- U$512: device output:OR0 -> output:3V30
- U$514: device output:GR0 -> output:VDD0
- U$515: device output:BLW0 -> output:A#0
- U$516: device output:BL0 -> output:A#1
- U$517: device output:BRW0 -> output:B#0
- U$518: device output:BR0 -> output:B#1
- U$519: device output:GND0 -> output:E#0
- U$521: device output:3V30 -> output:#RJ45_COLORS#0
- U$522, U$643: device output:GND0 -> output:#PWR#0
- U$523: device output:VDD0 -> output:IO250
- U$524: device output:A#0 -> output:IO330
- U$525: device output:A#1 -> output:IO170
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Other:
- board text added: "v11"
- board text removed: "v10"
